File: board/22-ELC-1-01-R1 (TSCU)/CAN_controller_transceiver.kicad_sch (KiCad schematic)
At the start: 15 parts, among them U7 MCP2515-xSO, U8 SN65HVD230, Y1 16 MHz

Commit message: Ready for review
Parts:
- renumbered C14 to C2, C15 to C3, C16 to C4, C17 to C5, R26 to R5, R30 to R6, TP8 to TP1, TP9 to TP2, TP10 to TP3, TP11 to TP4, TP12 to TP5, TP13 to TP6, U7 to U1, U8 to U2
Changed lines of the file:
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@@
   (symbol (lib_id "Device:C_Small") (at 152.4 92.71 270) (unit 1)
     (in_bom yes) (on_board yes)
-    (property "Reference" "C17" (id 0) (at 153.5684 95.0468 0)
+    (property "Reference" "C5" (id 0) (at 153.5684 95.0468 0)
       (effects (font (size 1.27 1.27)) (justify left))
     )
@@
   (symbol (lib_id "power:GND") (at 148.59 118.11 0) (unit 1)
     (in_bom yes) (on_board yes)
-    (property "Reference" "#PWR072" (id 0) (at 148.59 124.46 0)
+    (property "Reference" "#PWR028" (id 0) (at 148.59 124.46 0)
       (effects (font (size 1.27 1.27)) hide)
     )
@@
   (symbol (lib_id "power:GND") (at 157.48 93.98 0) (unit 1)
     (in_bom yes) (on_board yes)
-    (property "Reference" "#PWR073" (id 0) (at 157.48 100.33 0)
+    (property "Reference" "#PWR029" (id 0) (at 157.48 100.33 0)
       (effects (font (size 1.27 1.27)) hide)
     )
@@
   (symbol (lib_id "power:GND") (at 132.08 113.03 270) (unit 1)
     (in_bom yes) (on_board yes)
-    (property "Reference" "#PWR070" (id 0) (at 125.73 113.03 0)
+    (property "Reference" "#PWR026" (id 0) (at 125.73 113.03 0)
       (effects (font (size 1.27 1.27)) hide)
     )
@@
   (symbol (lib_id "Interface_CAN_LIN:MCP2515-xSO") (at 83.82 119.38 0) (unit 1)
     (in_bom yes) (on_board yes)
-    (property "Reference" "U7" (id 0) (at 72.39 100.33 0))
+    (property "Reference" "U1" (id 0) (at 72.39 100.33 0))
     (property "Value" "MCP2515-xSO" (id 1) (at 91.44 100.33 0))
     (property "Footprint" "Package_SO:SOIC-18W_7.5x11.6mm_P1.27mm" (id 2) (at 83.82 142.24 0)
@@
   (symbol (lib_id "Interface_CAN_LIN:SN65HVD230") (at 148.59 107.95 0) (unit 1)
     (in_bom yes) (on_board yes)
-    (property "Reference" "U8" (id 0) (at 142.24 101.6 0))
+    (property "Reference" "U2" (id 0) (at 142.24 101.6 0))
     (property "Value" "SN65HVD230" (id 1) (at 155.575 101.6 0))
     (property "Footprint" "Package_SO:SOIC-8_3.9x4.9mm_P1.27mm" (id 2) (at 148.59 120.65 0)
@@
   (symbol (lib_id "power:GND") (at 83.82 139.7 0) (unit 1)
     (in_bom yes) (on_board yes)
-    (property "Reference" "#PWR067" (id 0) (at 83.82 146.05 0)
+    (property "Reference" "#PWR022" (id 0) (at 83.82 146.05 0)
       (effects (font (size 1.27 1.27)) hide)
     )
@@
   (symbol (lib_id "power:GND") (at 45.72 125.73 0) (unit 1)
     (in_bom yes) (on_board yes)
-    (property "Reference" "#PWR063" (id 0) (at 45.72 132.08 0)
+    (property "Reference" "#PWR018" (id 0) (at 45.72 132.08 0)
       (effects (font (size 1.27 1.27)) hide)
     )
@@
   (symbol (lib_id "power:GND") (at 55.88 125.73 0) (unit 1)
     (in_bom yes) (on_board yes)
-    (property "Reference" "#PWR064" (id 0) (at 55.88 132.08 0)
+    (property "Reference" "#PWR019" (id 0) (at 55.88 132.08 0)
       (effects (font (size 1.27 1.27)) hide)
     )
@@
   (symbol (lib_id "Device:C_Small") (at 36.83 123.19 180) (unit 1)
     (in_bom yes) (on_board yes)
-    (property "Reference" "C14" (id 0) (at 37.465 120.015 0))
+    (property "Reference" "C2" (id 0) (at 37.465 120.015 0))
     (property "Value" "22pf" (id 1) (at 40.005 125.095 0))
     (property "Footprint" "Capacitor_SMD:C_0603_1608Metric_Pad1.08x0.95mm_HandSolder" (id 2) (at 36.83 123.19 0)
@@
   (symbol (lib_id "Device:C_Small") (at 36.83 128.27 180) (unit 1)
     (in_bom yes) (on_board yes)
-    (property "Reference" "C15" (id 0) (at 37.465 132.08 0))
+    (property "Reference" "C3" (id 0) (at 37.465 132.08 0))
     (property "Value" "22pf" (id 1) (at 40.005 127 0))
     (property "Footprint" "Capacitor_SMD:C_0603_1608Metric_Pad1.08x0.95mm_HandSolder" (id 2) (at 36.83 128.27 0)
@@
   (symbol (lib_id "power:GND") (at 31.75 125.73 0) (unit 1)
     (in_bom yes) (on_board yes)
-    (property "Reference" "#PWR062" (id 0) (at 31.75 132.08 0)
+    (property "Reference" "#PWR017" (id 0) (at 31.75 132.08 0)
       (effects (font (size 1.27 1.27)) hide)
     )
@@
   (symbol (lib_id "Connector:TestPoint") (at 67.31 104.14 0) (unit 1)
     (in_bom yes) (on_board yes)
-    (property "Reference" "TP11" (id 0) (at 66.04 99.06 0)
+    (property "Reference" "TP4" (id 0) (at 66.04 99.06 0)
       (effects (font (size 1.27 1.27)) (justify left))
     )
@@
   (symbol (lib_id "Device:C_Small") (at 87.63 92.71 270) (unit 1)
     (in_bom yes) (on_board yes)
-    (property "Reference" "C16" (id 0) (at 88.7984 95.0468 0)
+    (property "Reference" "C4" (id 0) (at 88.7984 95.0468 0)
       (effects (font (size 1.27 1.27)) (justify left))
     )
@@
   (symbol (lib_id "power:GND") (at 92.71 93.98 0) (unit 1)
     (in_bom yes) (on_board yes)
-    (property "Reference" "#PWR068" (id 0) (at 92.71 100.33 0)
+    (property "Reference" "#PWR023" (id 0) (at 92.71 100.33 0)
       (effects (font (size 1.27 1.27)) hide)
     )
@@
   (symbol (lib_id "power:+5V") (at 148.59 91.44 0) (unit 1)
     (in_bom yes) (on_board yes)
-    (property "Reference" "#PWR071" (id 0) (at 148.59 95.25 0)
+    (property "Reference" "#PWR027" (id 0) (at 148.59 95.25 0)
       (effects (font (size 1.27 1.27)) hide)
     )
@@
   (symbol (lib_id "power:+5V") (at 132.08 110.49 90) (unit 1)
     (in_bom yes) (on_board yes)
-    (property "Reference" "#PWR069" (id 0) (at 135.89 110.49 0)
+    (property "Reference" "#PWR025" (id 0) (at 135.89 110.49 0)
       (effects (font (size 1.27 1.27)) hide)
     )
@@
   (symbol (lib_id "power:+5V") (at 83.82 90.17 0) (unit 1)
     (in_bom yes) (on_board yes)
-    (property "Reference" "#PWR066" (id 0) (at 83.82 93.98 0)
+    (property "Reference" "#PWR021" (id 0) (at 83.82 93.98 0)
       (effects (font (size 1.27 1.27)) hide)
     )
@@
   (symbol (lib_id "Device:R") (at 57.15 91.44 0) (unit 1)
     (in_bom yes) (on_board yes)
-    (property "Reference" "R26" (id 0) (at 57.15 87.63 0)
+    (property "Reference" "R5" (id 0) (at 57.15 87.63 0)
       (effects (font (size 1.27 1.27)) (justify left))
     )
@@
   (symbol (lib_id "power:+5V") (at 57.15 87.63 0) (unit 1)
     (in_bom yes) (on_board yes)
-    (property "Reference" "#PWR065" (id 0) (at 57.15 91.44 0)
+    (property "Reference" "#PWR020" (id 0) (at 57.15 91.44 0)
       (effects (font (size 1.27 1.27)) hide)
     )
@@
   (symbol (lib_id "Connector:TestPoint") (at 64.77 101.6 0) (unit 1)
     (in_bom yes) (on_board yes)
-    (property "Reference" "TP10" (id 0) (at 63.5 96.52 0)
+    (property "Reference" "TP3" (id 0) (at 63.5 96.52 0)
       (effects (font (size 1.27 1.27)) (justify left))
     )
@@
   (symbol (lib_id "Connector:TestPoint") (at 62.23 99.06 0) (unit 1)
     (in_bom yes) (on_board yes)
-    (property "Reference" "TP9" (id 0) (at 60.96 93.98 0)
+    (property "Reference" "TP2" (id 0) (at 60.96 93.98 0)
       (effects (font (size 1.27 1.27)) (justify left))
     )
@@
   (symbol (lib_id "Connector:TestPoint") (at 59.69 96.52 0) (unit 1)
     (in_bom yes) (on_board yes)
-    (property "Reference" "TP8" (id 0) (at 58.42 91.44 0)
+    (property "Reference" "TP1" (id 0) (at 58.42 91.44 0)
       (effects (font (size 1.27 1.27)) (justify left))
     )
@@
   (symbol (lib_id "Connector:TestPoint") (at 121.92 105.41 0) (unit 1)
     (in_bom yes) (on_board yes)
-    (property "Reference" "TP12" (id 0) (at 120.65 100.33 0)
+    (property "Reference" "TP5" (id 0) (at 120.65 100.33 0)
       (effects (font (size 1.27 1.27)) (justify left))
     )
@@
   (symbol (lib_id "Connector:TestPoint") (at 125.73 104.14 0) (unit 1)
     (in_bom yes) (on_board yes)
-    (property "Reference" "TP13" (id 0) (at 124.46 99.06 0)
+    (property "Reference" "TP6" (id 0) (at 124.46 99.06 0)
       (effects (font (size 1.27 1.27)) (justify left))
     )
@@
   (symbol (lib_id "power:+5V") (at 109.22 125.73 0) (unit 1)
     (in_bom yes) (on_board yes)
-    (property "Reference" "#PWR080" (id 0) (at 109.22 129.54 0)
+    (property "Reference" "#PWR024" (id 0) (at 109.22 129.54 0)
       (effects (font (size 1.27 1.27)) hide)
     )
@@
   (symbol (lib_id "Device:R") (at 109.22 129.54 0) (unit 1)
     (in_bom yes) (on_board yes)
-    (property "Reference" "R30" (id 0) (at 110.998 128.3716 0)
-      (effects (font (size 1.27 1.27)) (justify left))
-    )
+    (property "Reference" "R6" (id 0) (at 110.998 128.3716 0)
+      (effects (font (size 1.27 1.27)) (justify left))
+    )

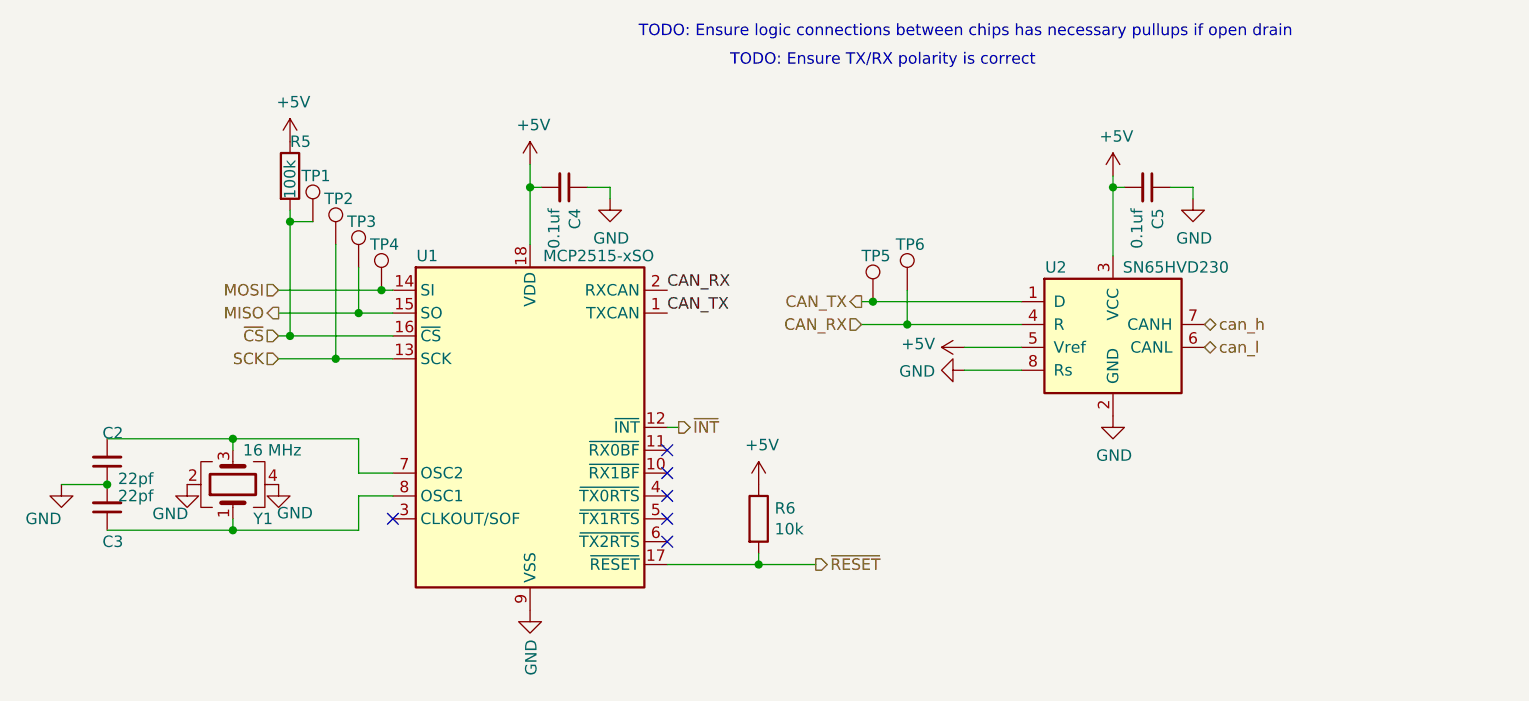
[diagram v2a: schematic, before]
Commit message: All good except need to switch everything to accepting 24v power
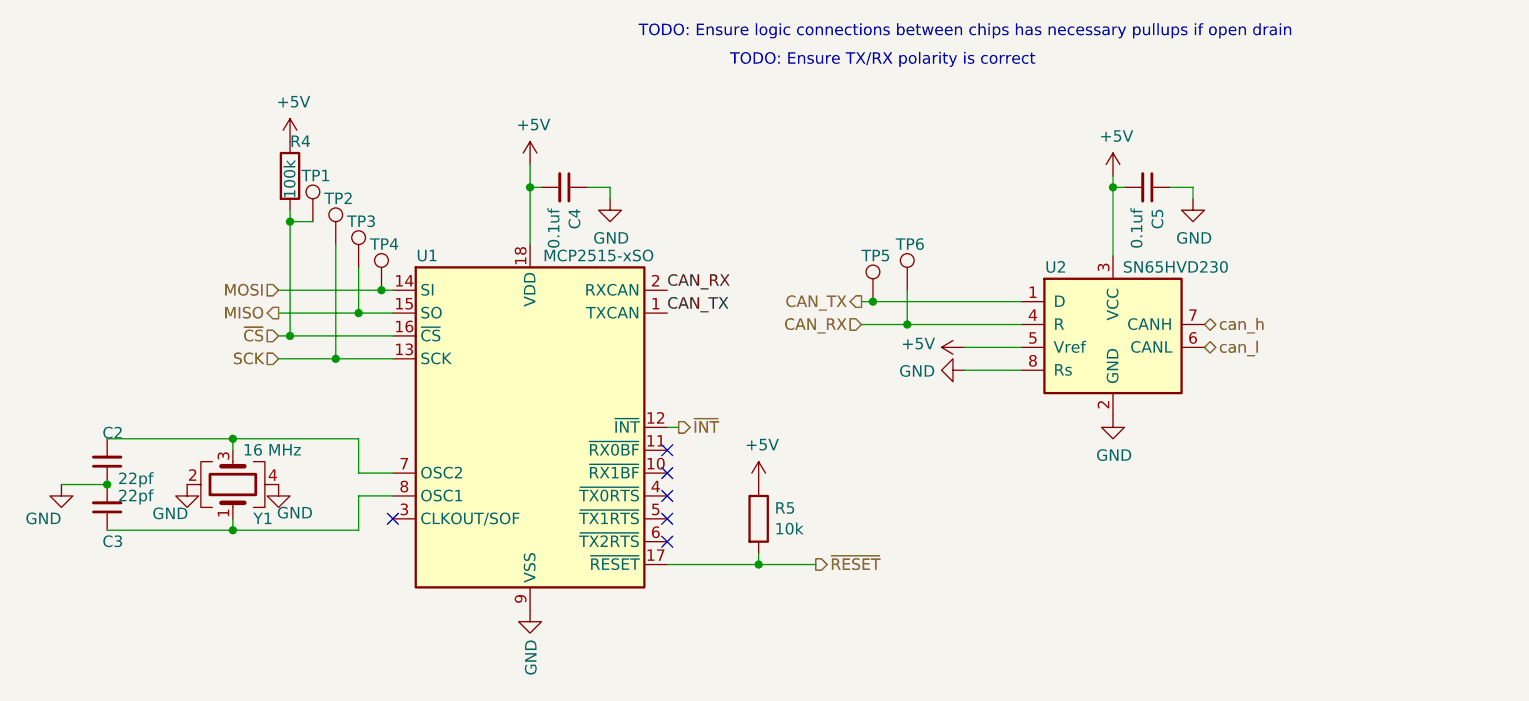
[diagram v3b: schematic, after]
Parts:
- R5: renamed from R6; footprint (none) -> Resistor_SMD:R_0603_1608Metric_Pad0.98x0.95mm_HandSolder
- renumbered R5 to R4
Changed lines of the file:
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@@
   (symbol (lib_id "power:GND") (at 148.59 118.11 0) (unit 1)
     (in_bom yes) (on_board yes)
-    (property "Reference" "#PWR028" (id 0) (at 148.59 124.46 0)
+    (property "Reference" "#PWR029" (id 0) (at 148.59 124.46 0)
       (effects (font (size 1.27 1.27)) hide)
     )
@@
   (symbol (lib_id "power:GND") (at 157.48 93.98 0) (unit 1)
     (in_bom yes) (on_board yes)
-    (property "Reference" "#PWR029" (id 0) (at 157.48 100.33 0)
+    (property "Reference" "#PWR030" (id 0) (at 157.48 100.33 0)
       (effects (font (size 1.27 1.27)) hide)
     )
@@
   (symbol (lib_id "power:GND") (at 132.08 113.03 270) (unit 1)
     (in_bom yes) (on_board yes)
-    (property "Reference" "#PWR026" (id 0) (at 125.73 113.03 0)
+    (property "Reference" "#PWR027" (id 0) (at 125.73 113.03 0)
       (effects (font (size 1.27 1.27)) hide)
     )
@@
   (symbol (lib_id "power:GND") (at 83.82 139.7 0) (unit 1)
     (in_bom yes) (on_board yes)
-    (property "Reference" "#PWR022" (id 0) (at 83.82 146.05 0)
+    (property "Reference" "#PWR023" (id 0) (at 83.82 146.05 0)
       (effects (font (size 1.27 1.27)) hide)
     )
@@
   (symbol (lib_id "power:GND") (at 45.72 125.73 0) (unit 1)
     (in_bom yes) (on_board yes)
-    (property "Reference" "#PWR018" (id 0) (at 45.72 132.08 0)
+    (property "Reference" "#PWR019" (id 0) (at 45.72 132.08 0)
       (effects (font (size 1.27 1.27)) hide)
     )
@@
   (symbol (lib_id "power:GND") (at 55.88 125.73 0) (unit 1)
     (in_bom yes) (on_board yes)
-    (property "Reference" "#PWR019" (id 0) (at 55.88 132.08 0)
+    (property "Reference" "#PWR020" (id 0) (at 55.88 132.08 0)
       (effects (font (size 1.27 1.27)) hide)
     )
@@
   (symbol (lib_id "power:GND") (at 31.75 125.73 0) (unit 1)
     (in_bom yes) (on_board yes)
-    (property "Reference" "#PWR017" (id 0) (at 31.75 132.08 0)
+    (property "Reference" "#PWR018" (id 0) (at 31.75 132.08 0)
       (effects (font (size 1.27 1.27)) hide)
     )
@@
   (symbol (lib_id "power:GND") (at 92.71 93.98 0) (unit 1)
     (in_bom yes) (on_board yes)
-    (property "Reference" "#PWR023" (id 0) (at 92.71 100.33 0)
+    (property "Reference" "#PWR024" (id 0) (at 92.71 100.33 0)
       (effects (font (size 1.27 1.27)) hide)
     )
@@
   (symbol (lib_id "power:+5V") (at 148.59 91.44 0) (unit 1)
     (in_bom yes) (on_board yes)
-    (property "Reference" "#PWR027" (id 0) (at 148.59 95.25 0)
+    (property "Reference" "#PWR028" (id 0) (at 148.59 95.25 0)
       (effects (font (size 1.27 1.27)) hide)
     )
@@
   (symbol (lib_id "power:+5V") (at 132.08 110.49 90) (unit 1)
     (in_bom yes) (on_board yes)
-    (property "Reference" "#PWR025" (id 0) (at 135.89 110.49 0)
+    (property "Reference" "#PWR026" (id 0) (at 135.89 110.49 0)
       (effects (font (size 1.27 1.27)) hide)
     )
@@
   (symbol (lib_id "power:+5V") (at 83.82 90.17 0) (unit 1)
     (in_bom yes) (on_board yes)
-    (property "Reference" "#PWR021" (id 0) (at 83.82 93.98 0)
+    (property "Reference" "#PWR022" (id 0) (at 83.82 93.98 0)
       (effects (font (size 1.27 1.27)) hide)
     )
@@
   (symbol (lib_id "Device:R") (at 57.15 91.44 0) (unit 1)
     (in_bom yes) (on_board yes)
-    (property "Reference" "R5" (id 0) (at 57.15 87.63 0)
+    (property "Reference" "R4" (id 0) (at 57.15 87.63 0)
       (effects (font (size 1.27 1.27)) (justify left))
     )
@@
   (symbol (lib_id "power:+5V") (at 57.15 87.63 0) (unit 1)
     (in_bom yes) (on_board yes)
-    (property "Reference" "#PWR020" (id 0) (at 57.15 91.44 0)
+    (property "Reference" "#PWR021" (id 0) (at 57.15 91.44 0)
       (effects (font (size 1.27 1.27)) hide)
     )
@@
   (symbol (lib_id "power:+5V") (at 109.22 125.73 0) (unit 1)
     (in_bom yes) (on_board yes)
-    (property "Reference" "#PWR024" (id 0) (at 109.22 129.54 0)
+    (property "Reference" "#PWR025" (id 0) (at 109.22 129.54 0)
       (effects (font (size 1.27 1.27)) hide)
     )
@@
   (symbol (lib_id "Device:R") (at 109.22 129.54 0) (unit 1)
     (in_bom yes) (on_board yes)
-    (property "Reference" "R6" (id 0) (at 110.998 128.3716 0)
+    (property "Reference" "R5" (id 0) (at 110.998 128.3716 0)
       (effects (font (size 1.27 1.27)) (justify left))
     )
@@
       (effects (font (size 1.27 1.27)) (justify left))
     )
-    (property "Footprint" "" (id 2) (at 107.442 129.54 90)
-      (effects (font (size 1.27 1.27)) hide)
-    )
+    (property "Footprint" "Resistor_SMD:R_0603_1608Metric_Pad0.98x0.95mm_HandSolder" (id 2) (at 107.442 129.54 90)
+      (effects (font (size 1.27 1.27)) hide)
+    )
